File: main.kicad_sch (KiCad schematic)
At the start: 39 parts, among them Q2 AO4407A, U11 SAM-M10Q-00B, U12 BMP581, U2 TPS543620RPYR, U4 BNO085

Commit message: Updated BOM
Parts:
- L1: Distributor Link (none) -> https://www.digikey.com/en/products/detail/w%C3%BCrth-elekt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; Manufacturer Part Number (none) -> 744325240
- Q2: Distributor Link (none) -> https://www.digikey.com/en/products/detail/alpha-omega-semi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; Manufacturer Part Number (none) -> AO4407A
- U2: Distributor Link (none) -> https://www.digikey.com/en/products/detail/texas-instrument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; Manufacturer Part Number (none) -> TPS543620RPYR
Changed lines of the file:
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@@
 			)
 		)
+		(property "Distributor Link" "https://www.digikey.com/en/products/detail/w%C3%BCrth-elektronik/744325240/1638573?s=N4IgTCBcDaIOwBYEGYwFYwIAwgLoF8g"
+			(at 205.74 109.22 90)
+			(hide yes)
+			(show_name no)
+			(do_not_autoplace no)
+			(effects
+				(font
+					(size 1.27 1.27)
+				)
+			)
+		)
+		(property "Manufacturer Part Number" "744325240"
+			(at 205.74 109.22 90)
+			(hide yes)
+			(show_name no)
+			(do_not_autoplace no)
+			(effects
+				(font
+					(size 1.27 1.27)
+				)
+			)
+		)
 		(pin "1"
 		)
@@
 			)
 		)
+		(property "Distributor Link" "https://www.digikey.com/en/products/detail/texas-instruments/TPS543620RPYR/13563030?s=N4IgTCBcDaICoAUDKBWALAZgGxgAwCUEBNfAYThAF0BfIA"
+			(at 160.02 106.68 0)
+			(hide yes)
+			(show_name no)
+			(do_not_autoplace no)
+			(effects
+				(font
+					(size 1.27 1.27)
+				)
+			)
+		)
+		(property "Manufacturer Part Number" "TPS543620RPYR"
+			(at 160.02 106.68 0)
+			(hide yes)
+			(show_name no)
+			(do_not_autoplace no)
+			(effects
+				(font
+					(size 1.27 1.27)
+				)
+			)
+		)
 		(pin "1"
 		)
@@
 			)
 		)
+		(property "Distributor Link" "https://www.digikey.com/en/products/detail/alpha-omega-semiconductor-inc/AO4407A/1855794"
+			(at 64.77 113.03 0)
+			(hide yes)
+			(show_name no)
+			(do_not_autoplace no)
+			(effects
+				(font
+					(size 1.27 1.27)
+				)
+			)
+		)
+		(property "Manufacturer Part Number" "AO4407A"
+			(at 64.77 113.03 0)
+			(hide yes)
+			(show_name no)
+			(do_not_autoplace no)
+			(effects
+				(font
+					(size 1.27 1.27)
+				)
+			)
+		)

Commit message: Final BOM
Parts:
- C19, C20, C21, C24, C25, C26, C28, C31, C34: Distributor Link (none) -> https://www.digikey.com/en/products/detail/kemet/C0603C104K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; Manufacturer Part Number (none) -> C0603C104K5RACTU
- C27: Distributor Link (none) -> https://www.digikey.com/en/products/detail/murata-electroni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; Manufacturer Part Number (none) -> GRM188R61E106MA73D
- C30, C32, C33, C37, C38: Distributor Link (none) -> https://www.digikey.com/en/products/detail/murata-electroni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; Manufacturer Part Number (none) -> GRM188R61E475KE11D
- C35: Distributor Link (none) -> https://www.digikey.com/en/products/detail/yageo/CC0603JRNP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; Manufacturer Part Number (none) -> CC0603JRNPO9BN150
- C36, C39: Distributor Link (none) -> https://www.digikey.com/en/products/detail/murata-electroni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; Manufacturer Part Number (none) -> GRM188R60J476ME15D
- R14, R19, R20, R24, R27, R28, R29, R35: footprint Capacitor_SMD:C_0603_1608Metric -> Resistor_SMD:R_0603_1608Metric; Distributor Link (none) -> https://www.digikey.com/en/products/detail/yageo/RC0603JR-0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; Manufacturer Part Number (none) -> RC0603JR-0710KL
- R17, R18: footprint Capacitor_SMD:C_0603_1608Metric -> Resistor_SMD:R_0603_1608Metric; Distributor Link (none) -> https://www.digikey.com/en/products/detail/yageo/RC0603FR-0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; Manufacturer Part Number (none) -> RC0603FR-074K7L
- R21: footprint Capacitor_SMD:C_0603_1608Metric -> Resistor_SMD:R_0603_1608Metric; Distributor Link (none) -> https://www.digikey.com/en/products/detail/yageo/RC0603FR-0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; Manufacturer Part Number (none) -> RC0603FR-07100KL
- R25: footprint Capacitor_SMD:C_0603_1608Metric -> Resistor_SMD:R_0603_1608Metric; Distributor Link (none) -> https://www.digikey.com/en/products/detail/yageo/RT0603BRD0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; Manufacturer Part Number (none) -> RT0603BRD0711K3L
- R26: footprint Capacitor_SMD:C_0603_1608Metric -> Resistor_SMD:R_0603_1608Metric; Distributor Link (none) -> https://www.digikey.com/en/products/detail/yageo/RC0603FR-0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; Manufacturer Part Number (none) -> RC0603FR-0724K3L
- R34: footprint Capacitor_SMD:C_0603_1608Metric -> Resistor_SMD:R_0603_1608Metric; Distributor Link (none) -> https://www.digikey.com/en/products/detail/bourns-inc/CR060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; Manufacturer Part Number (none) -> CR0603-FX-9092ELF

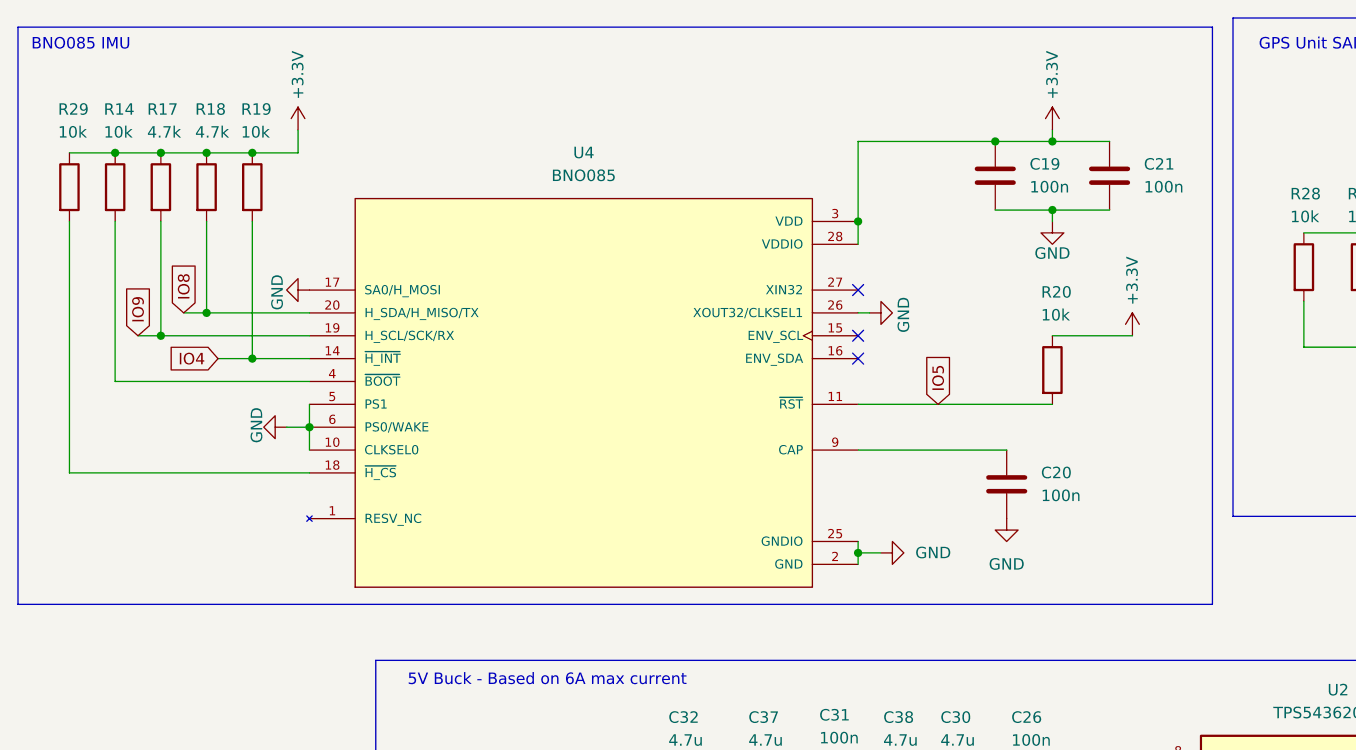
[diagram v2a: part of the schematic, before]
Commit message: BNO085 --> BNO055
Due to stock issues, the BNO085 was changed to a BNO055.

*Updated gerber, drill, pos files (IN ZIP FILE IN MANUFACTURING > 2027Payload_GBR_DRL_POS_V5)
*Updated schematic and PCB design
*Updated BOM
*Updated canva block diagrams
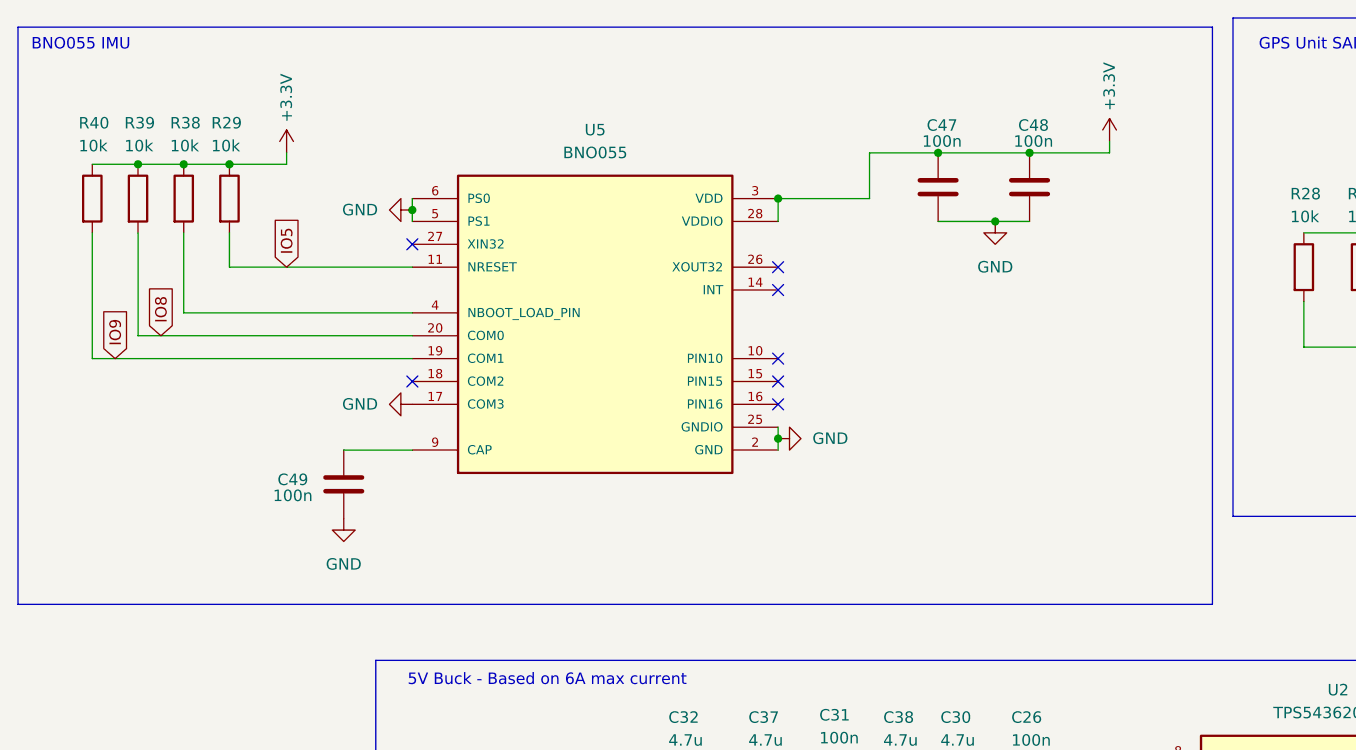
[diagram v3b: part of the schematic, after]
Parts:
- removed C19, C20, C21: 100n, Capacitor_SMD:C_0603_1608Metric, symbol Device:C
- removed R14, R19, R20: 10k, Resistor_SMD:R_0603_1608Metric, symbol Device:R
- removed R17, R18: 4.7k, Resistor_SMD:R_0603_1608Metric, symbol Device:R
- removed U4: BNO085, BNO085:IC_BNO085, symbol BNO085:BNO085
- added C47, C48, C49: 100n, Capacitor_SMD:C_0603_1608Metric, symbol Device:C
- added R38, R39, R40: 10k, Resistor_SMD:R_0603_1608Metric, symbol Device:R
- added U5: BNO055, BNO055:LGA28R50P4X10_380X520X100, symbol BNO055:BNO055
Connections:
- net +3.3V: now also C47.1, C48.1, R38.1, R39.1, R40.1, U5.28 (VDDIO), U5.3 (VDD)
- net GND: now also C47.2, C48.2, C49.2, U5.17 (COM3), U5.2 (GND), U5.25 (GNDIO), U5.5 (PS1), U5.6 (PS0)
- net IO5: now also R29.2, U5.11 (NRESET)
- net IO8: now also R39.2, U5.20 (COM0)
- net IO9: now also R40.2, U5.19 (COM1)
- new net: C49.1, U5.9 (CAP)
- new net: R38.2, U5.4 (NBOOT_LOAD_PIN)
- no-connect marks 9 -> 13
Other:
- note added: "BNO055 IMU"
- note removed: "BNO085 IMU"
